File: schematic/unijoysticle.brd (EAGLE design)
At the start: 49.5 x 49.5 mm, 6 parts, among them IC1 4066N, IC2 4066N, IC3 4066N, J1 DB9, J2 DB9

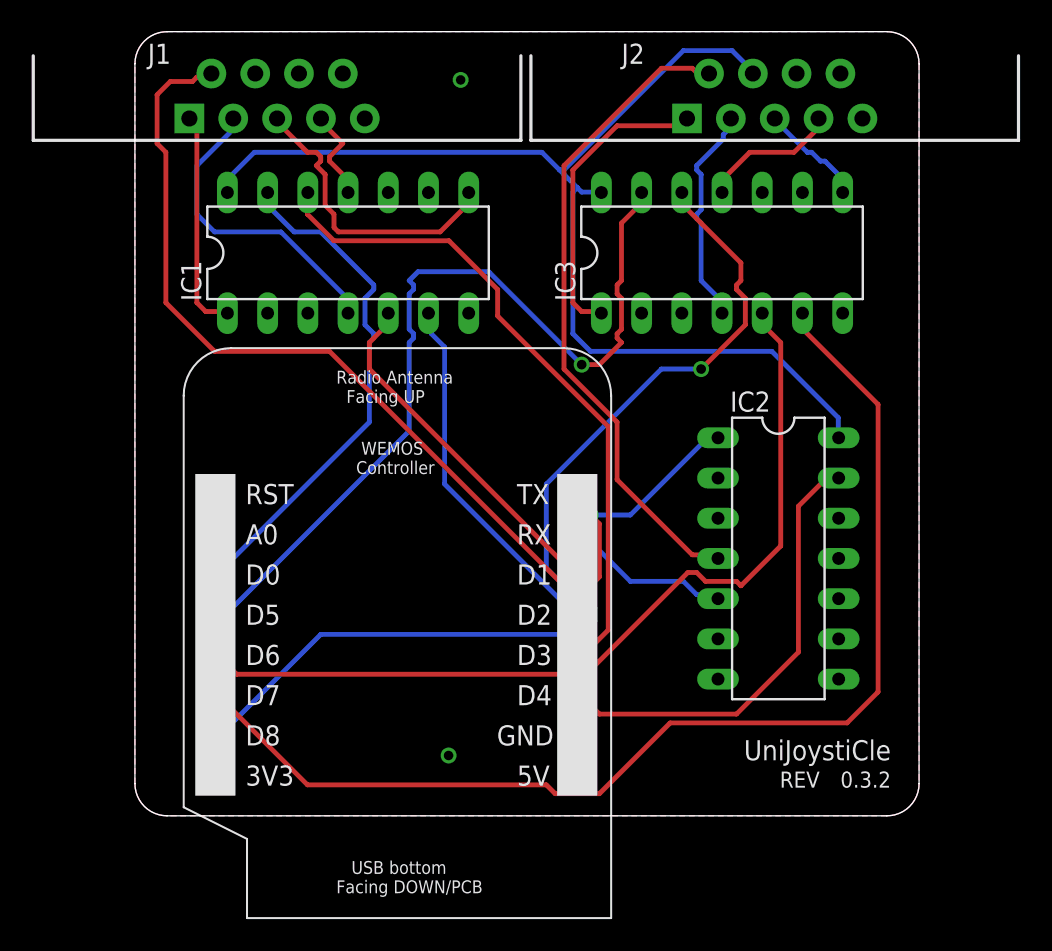
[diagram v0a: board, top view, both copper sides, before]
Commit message: fix: slightly better PCB design.
chip + D1 are placed a little bit better makeing it possible
to have a better routing
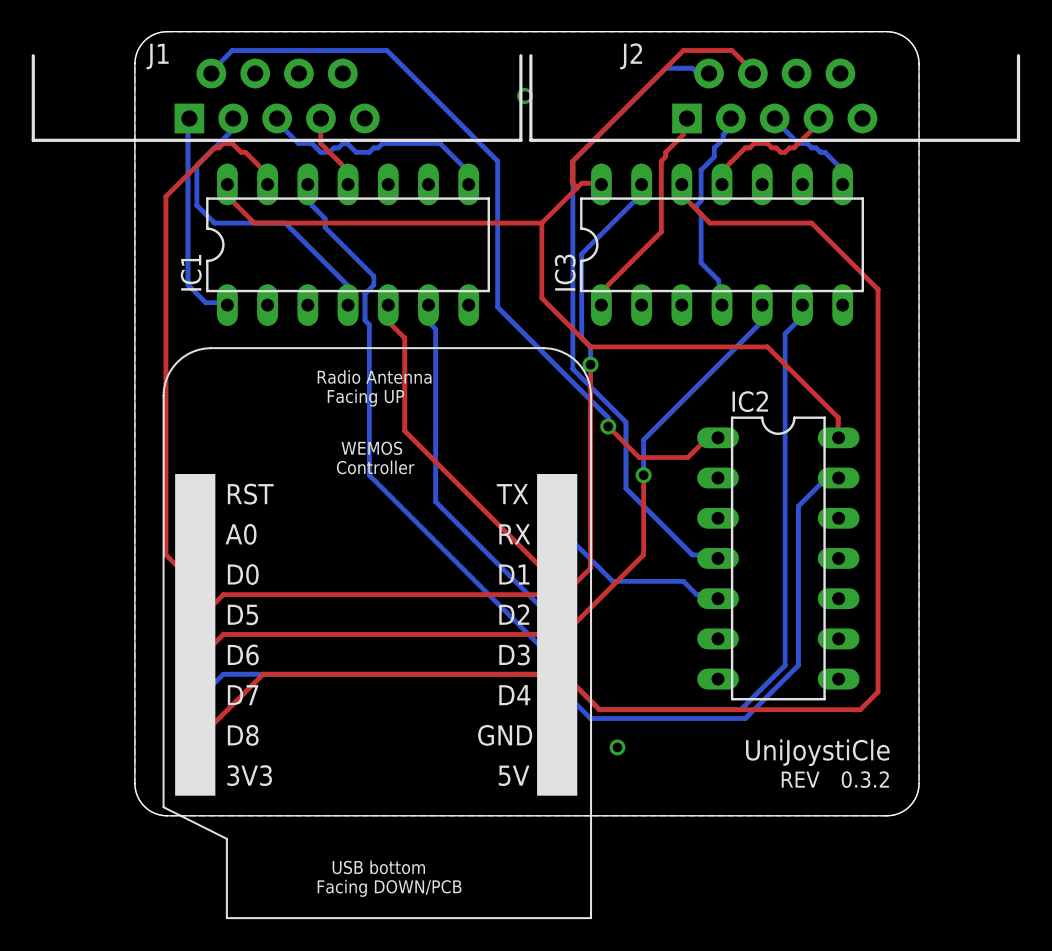
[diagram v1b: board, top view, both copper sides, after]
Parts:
- moved U$1 1.27 mm to (3.81, 2.54)
- moved IC1 0.51 mm to (13.5, 36.1)
- moved IC3 0.51 mm to (37.1, 36.1)
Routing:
- net J2RIGHT: track 64.2 -> 87.1 mm, vias 1 -> 0
- net N$21: track 67.1 -> 49.6 mm
- net J2LEFT: track 73.0 -> 63.2 mm
- net J2DOWN: track 55.4 -> 49.9 mm, vias 0 -> 1
- net J1RIGHT: track 42.5 -> 37.0 mm
- net N$13: track 19.0 -> 14.0 mm
- net N$11: track 19.0 -> 15.4 mm
- net J1FIRE: track 28.7 -> 30.6 mm
- net J2UP: track 54.1 -> 52.2 mm
- net J1UP: track 32.5 -> 34.2 mm
- net N$12: track 6.10 -> 4.88 mm
- net J2FIRE: track 10.7 -> 11.9 mm
- net VCC: track 71.9 -> 70.8 mm
- net J1DOWN: track 22.6 -> 21.8 mm
- net N$14: track 14.1 -> 13.4 mm
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
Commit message: board: add 5V barrel jack to board (again)
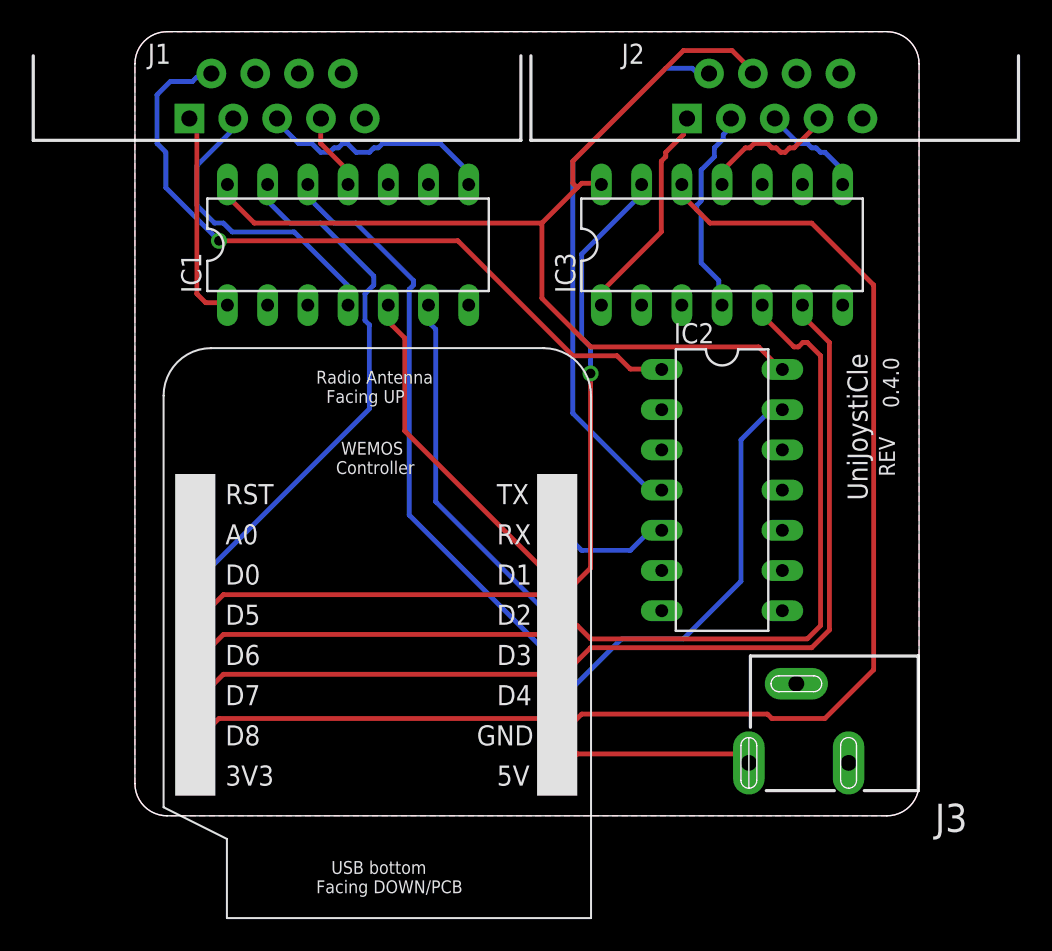
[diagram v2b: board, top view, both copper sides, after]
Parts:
- added J3: 5V ONLY, SparkFun-Connectors:POWER_JACK_SLOT
- moved IC2 5.59 mm to (37.1, 20.6)
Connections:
- new net 5V: J3.PWR, U$1.5V
- net GND: now also J3.GND@1, J3.GND@2
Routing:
- net J2DOWN: track 49.9 -> 63.6 mm, vias 1 -> 0
- net 5V: track 0.00 -> 12.9 mm
- net N$22: track 40.9 -> 34.7 mm
- net VCC: track 70.8 -> 64.7 mm
- net J2FIRE: track 11.9 -> 7.62 mm
- net J1FIRE: track 30.6 -> 27.0 mm
- net N$21: track 49.6 -> 46.2 mm
- net J2RIGHT: track 87.1 -> 84.5 mm
- net J1RIGHT: track 37.0 -> 37.6 mm

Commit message: board: missing via and better labels
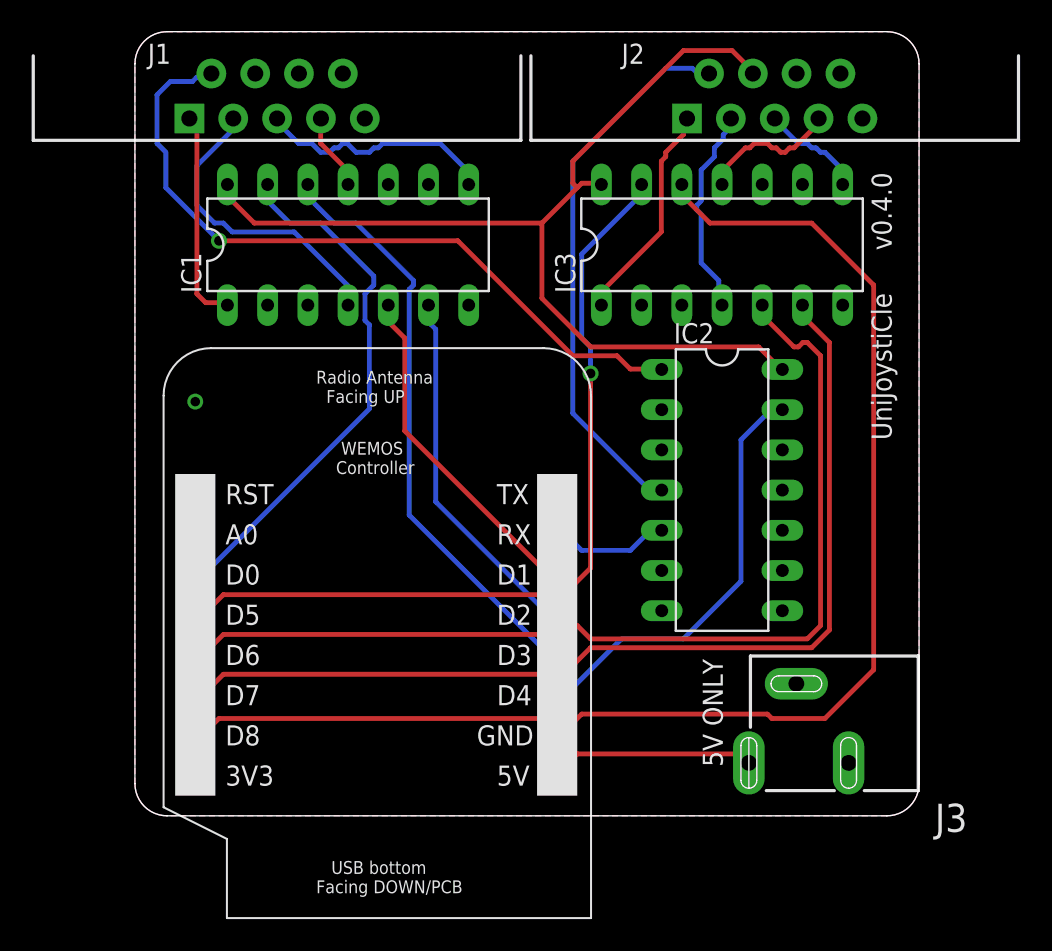
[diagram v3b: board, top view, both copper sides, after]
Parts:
- J3: value 5V ONLY -> POWER
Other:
- board text added: "5V ONLY"
- board text removed: "REV"
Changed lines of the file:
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@@
 <wire x1="47.498" y1="49.53" x2="2.032" y2="49.53" width="0" layer="20"/>
 <wire x1="2.032" y1="49.53" x2="0" y2="47.498" width="0" layer="20" curve="90"/>
-<text x="48.26" y="28.956" size="1.016" layer="21" rot="R270" align="top-left">&gt;REVISION</text>
+<text x="47.8028" y="40.64" size="1.27" layer="21" rot="R270" align="top-left">&gt;REVISION</text>
 <text x="23.6093" y="4.6355" size="1.27" layer="22" font="vector" rot="SMR270" align="top-right">http://retro.moe</text>
-<text x="48.006" y="23.9522" size="1.016" layer="21" rot="R270" align="top-left">REV</text>
-<text x="46.2788" y="29.21" size="1.27" layer="21" rot="R270" align="top-left">UniJoystiCle</text>
+<text x="47.8028" y="33.02" size="1.27" layer="21" rot="R270" align="top-left">UniJoystiCle</text>
 <rectangle x1="22.479" y1="20.3708" x2="22.7838" y2="20.447" layer="22" rot="R90"/>
 <rectangle x1="22.479" y1="20.828" x2="22.7838" y2="20.9042" layer="22" rot="R90"/>
@@
 <rectangle x1="7.239" y1="22.5044" x2="8.1534" y2="22.5806" layer="22" rot="R90"/>
 <rectangle x1="7.3152" y1="22.5044" x2="7.9248" y2="22.5806" layer="22" rot="R90"/>
+<text x="37.1348" y="9.906" size="1.27" layer="21" rot="R270" align="top-left">5V ONLY</text>
 </plain>
 <attributes>
-<attribute name="REVISION" value="0.4.0"/>
+<attribute name="REVISION" value="v0.4.0"/>
 </attributes>
 <variantdefs>
@@
 </element>
 <element name="U$1" library="1455413453956-wemos" package="WEMOS" value="WEMOS" x="3.81" y="2.54"/>
-<element name="J3" library="SparkFun-Connectors" package="POWER_JACK_SLOT" value="5V ONLY  " x="52.578" y="0.762" rot="R90">
+<element name="J3" library="SparkFun-Connectors" package="POWER_JACK_SLOT" value="POWER" x="52.578" y="0.762" rot="R90">
 <attribute name="PROD_ID" value="PRT-00119" x="52.578" y="0.762" size="1.778" layer="27" rot="R90" display="off"/>
 </element>
@@
 <wire x1="38.5572" y1="3.3528" x2="38.778" y2="3.342" width="0.3048" layer="1"/>
 </signal>
+<signal name="N$1">
+<via x="3.81" y="26.162" extent="1-16" drill="0.6" shape="square"/>
+</signal>
 </signals>

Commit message: schematic: adds diode again
I don't know if it is really needed, but it is scary
to see the c64 LED on, even if the computer is off
when the unijosyticle is being powered by USB,
but externally connected to the datassette port
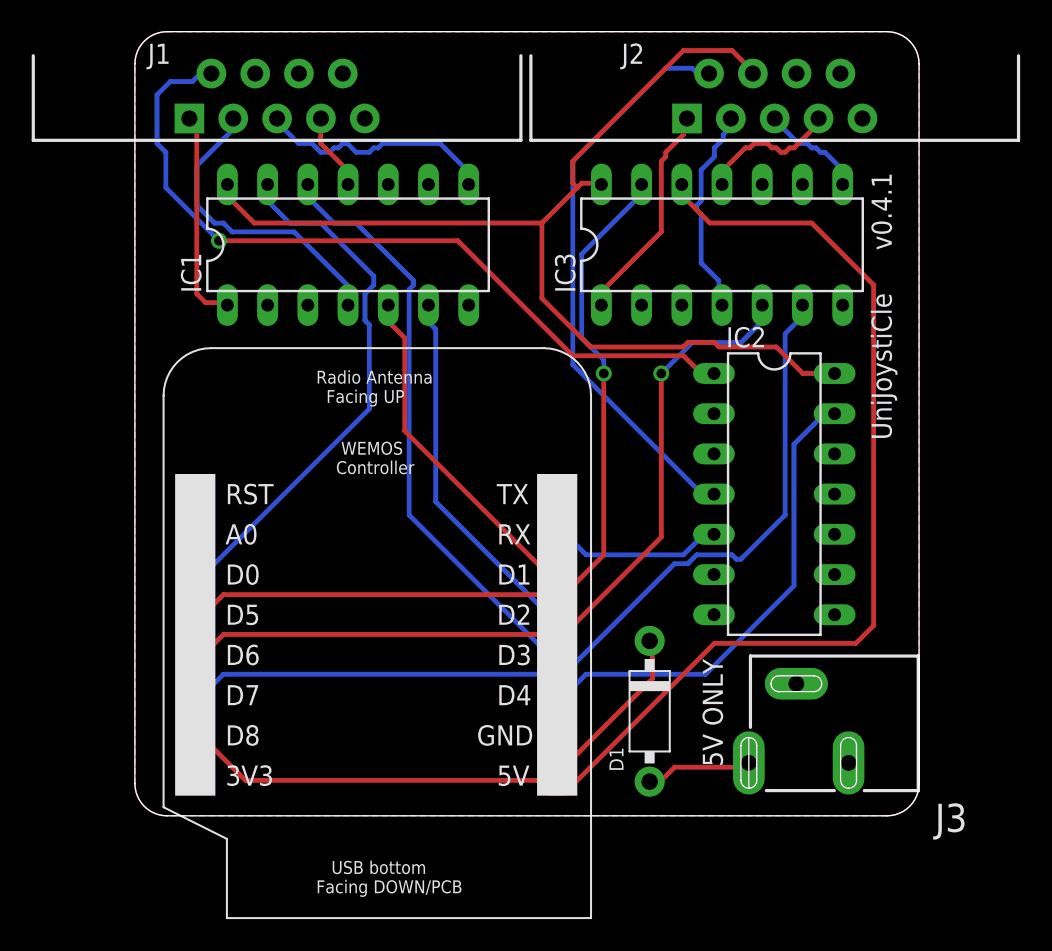
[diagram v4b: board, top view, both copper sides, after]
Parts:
- added D1: 1N4001, Seeed-OPL-Diode:DO-41
- moved IC2 3.31 mm to (40.4, 20.3)
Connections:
- removed net 5V: J3.PWR, U$1.5V
- new net EXT.5V: D1.2, U$1.5V
- new net N$1: D1.1, J3.PWR
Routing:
- net 5V: track 12.9 -> 0.00 mm
- net J2DOWN: track 63.6 -> 51.7 mm, vias 0 -> 1
- net EXT.5V: track 0.00 -> 11.1 mm
- net J2LEFT: track 63.0 -> 56.0 mm
- net N$1: track 0.00 -> 6.76 mm, vias 1 -> 0
- net VCC: track 64.7 -> 68.4 mm
- net N$21: track 46.2 -> 49.6 mm
- net J2FIRE: track 7.62 -> 11.0 mm
- net J1FIRE: track 27.0 -> 30.2 mm
- net N$22: track 34.7 -> 36.3 mm
- net J2RIGHT: track 84.5 -> 85.4 mm
- net J2UP: track 52.2 -> 52.9 mm
